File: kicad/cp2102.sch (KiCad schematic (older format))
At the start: 6 parts, among them CON1 USB-MINI-B, P1 CONN_6, U1 CP2102

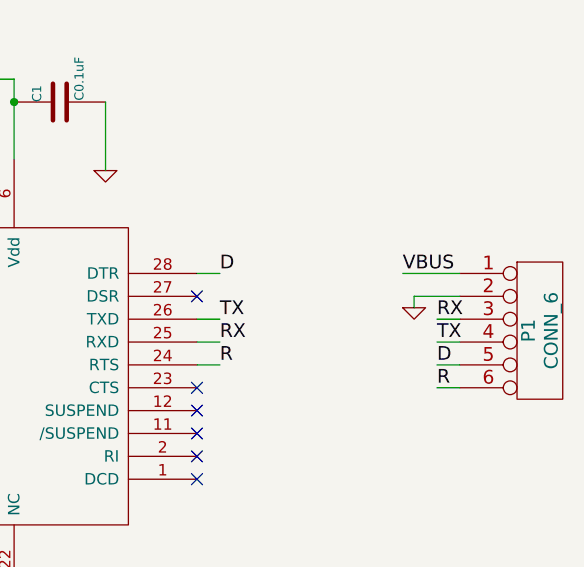
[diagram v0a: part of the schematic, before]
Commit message: Swpan power pins.
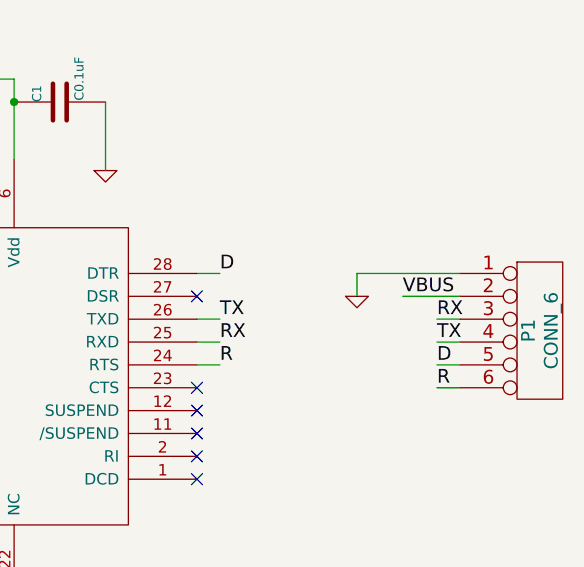
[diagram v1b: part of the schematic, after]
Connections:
- net GND: now also P1.1; no longer P1.2
- net VBUS: now also P1.2; no longer P1.1
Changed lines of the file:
@@
 Sheet 1 1
 Title ""
-Date "11 oct 2013"
+Date "12 oct 2013"
 Rev ""
 Comp ""
@@
 	1    0    0    -1
 $EndComp
-Text Label 8150 3200 0    60   ~ 0
-VBUS
-Wire Wire Line
-	8400 3200 8150 3200
+Text Label 8150 3300 0    60   ~ 0
+VBUS
+Wire Wire Line
+	7950 3200 8400 3200
 $Comp
 L GND #PWR7
 U 1 1 5256FCFC
-P 8200 3350
-F 0 "#PWR7" H 8200 3350 30  0001 C CNN
-F 1 "GND" H 8200 3280 30  0001 C CNN
-F 2 "" H 8200 3350 60  0000 C CNN
-F 3 "" H 8200 3350 60  0000 C CNN
-	1    8200 3350
-	1    0    0    -1
-$EndComp
-Wire Wire Line
-	8400 3300 8200 3300
-Wire Wire Line
-	8200 3300 8200 3350
+P 7950 3300
+F 0 "#PWR7" H 7950 3300 30  0001 C CNN
+F 1 "GND" H 7950 3230 30  0001 C CNN
+F 2 "" H 7950 3300 60  0000 C CNN
+F 3 "" H 7950 3300 60  0000 C CNN
+	1    7950 3300
+	1    0    0    -1
+$EndComp
 Text Label 8300 3400 0    60   ~ 0
 RX
@@
 Wire Wire Line
 	4650 2650 4650 2750
+Wire Wire Line
+	8150 3300 8400 3300
+Wire Wire Line
+	7950 3200 7950 3300
 $EndSCHEMATC
